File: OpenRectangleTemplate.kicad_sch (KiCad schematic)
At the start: 40 parts, among them J1 USB C Connector, J2 JTAG_TC2030, SW1 Boot, U1 XC6206, U2 USBLC6-2SC6, U3 RP2040, U4 W25Q128JVS, Y1 12MHz

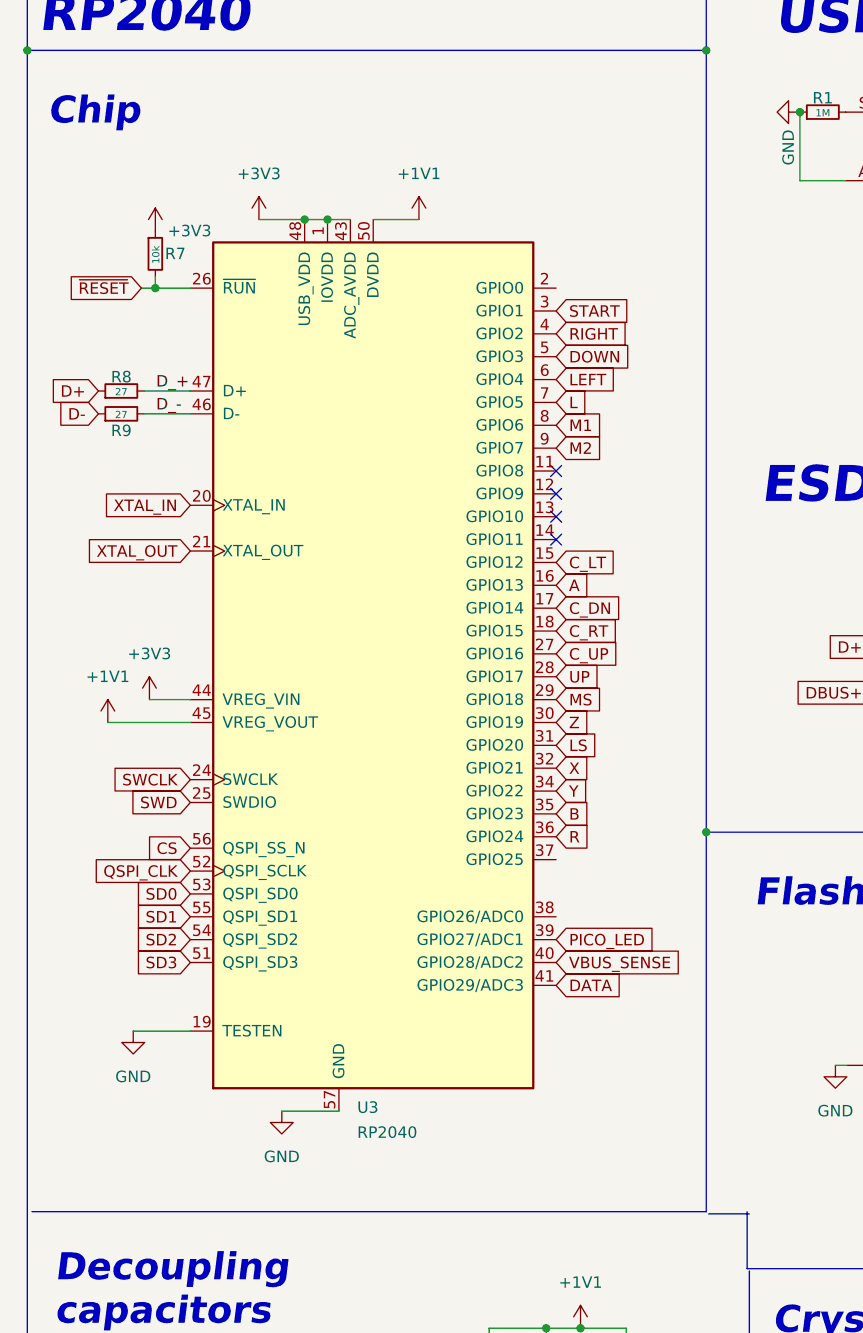
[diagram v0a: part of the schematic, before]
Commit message: Reverted back to pico pinout
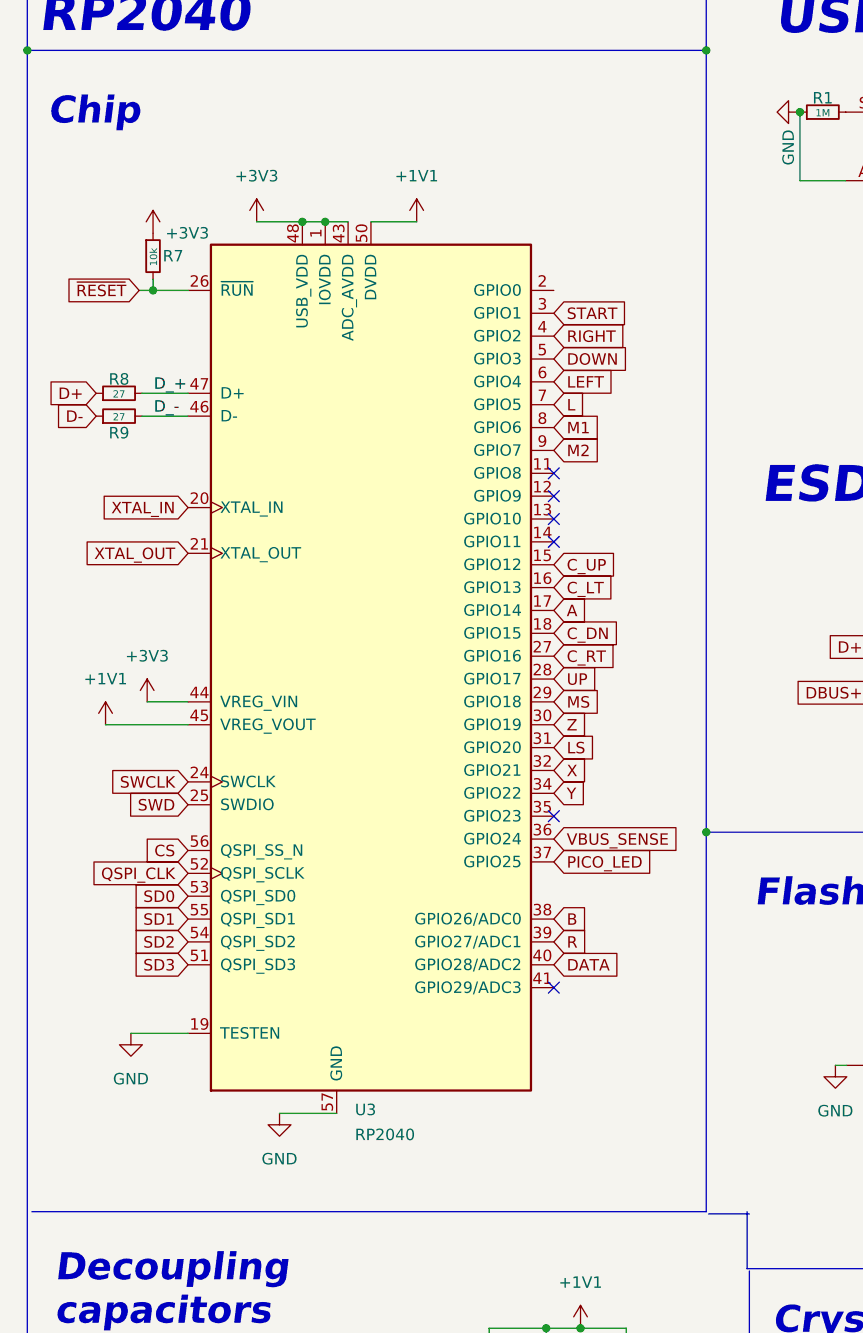
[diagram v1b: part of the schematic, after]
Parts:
- D1, D2: footprint qw-footprints:CUSTOM D_SOD-123 -> Diode_SMD:D_SOD-123
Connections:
- net A: now also U3.17 (GPIO14); no longer U3.16 (GPIO13)
- net B: now also U3.38 (GPIO26/ADC0); no longer U3.35 (GPIO23)
- net C_DN: now also U3.18 (GPIO15); no longer U3.17 (GPIO14)
- net C_LT: now also U3.16 (GPIO13); no longer U3.15 (GPIO12)
- net C_RT: now also U3.27 (GPIO16); no longer U3.18 (GPIO15)
- net C_UP: now also U3.15 (GPIO12); no longer U3.27 (GPIO16)
- net DATA: now also U3.40 (GPIO28/ADC2); no longer U3.41 (GPIO29/ADC3)
- net PICO_LED: now also U3.37 (GPIO25); no longer U3.39 (GPIO27/ADC1)
- net R: now also U3.39 (GPIO27/ADC1); no longer U3.36 (GPIO24)
- net VBUS_SENSE: now also U3.36 (GPIO24); no longer U3.40 (GPIO28/ADC2)
- no-connect marks 9 -> 11

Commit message: Prototyped and tested
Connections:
- net START: now also U3.2 (GPIO0); no longer U3.3 (GPIO1)
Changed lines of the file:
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@@
     )
   )
-  (global_label "START" (shape input) (at 71.7108 51.308 0) (fields_autoplaced)
+  (global_label "START" (shape input) (at 71.7108 48.768 0) (fields_autoplaced)
     (effects (font (size 1.27 1.27)) (justify left))
-    (property "Intersheetrefs" "${INTERSHEET_REFS}" (at 79.6272 51.2286 0)
+    (property "Intersheetrefs" "${INTERSHEET_REFS}" (at 79.6272 48.6886 0)
       (effects (font (size 1.27 1.27)) (justify left) hide)
     )

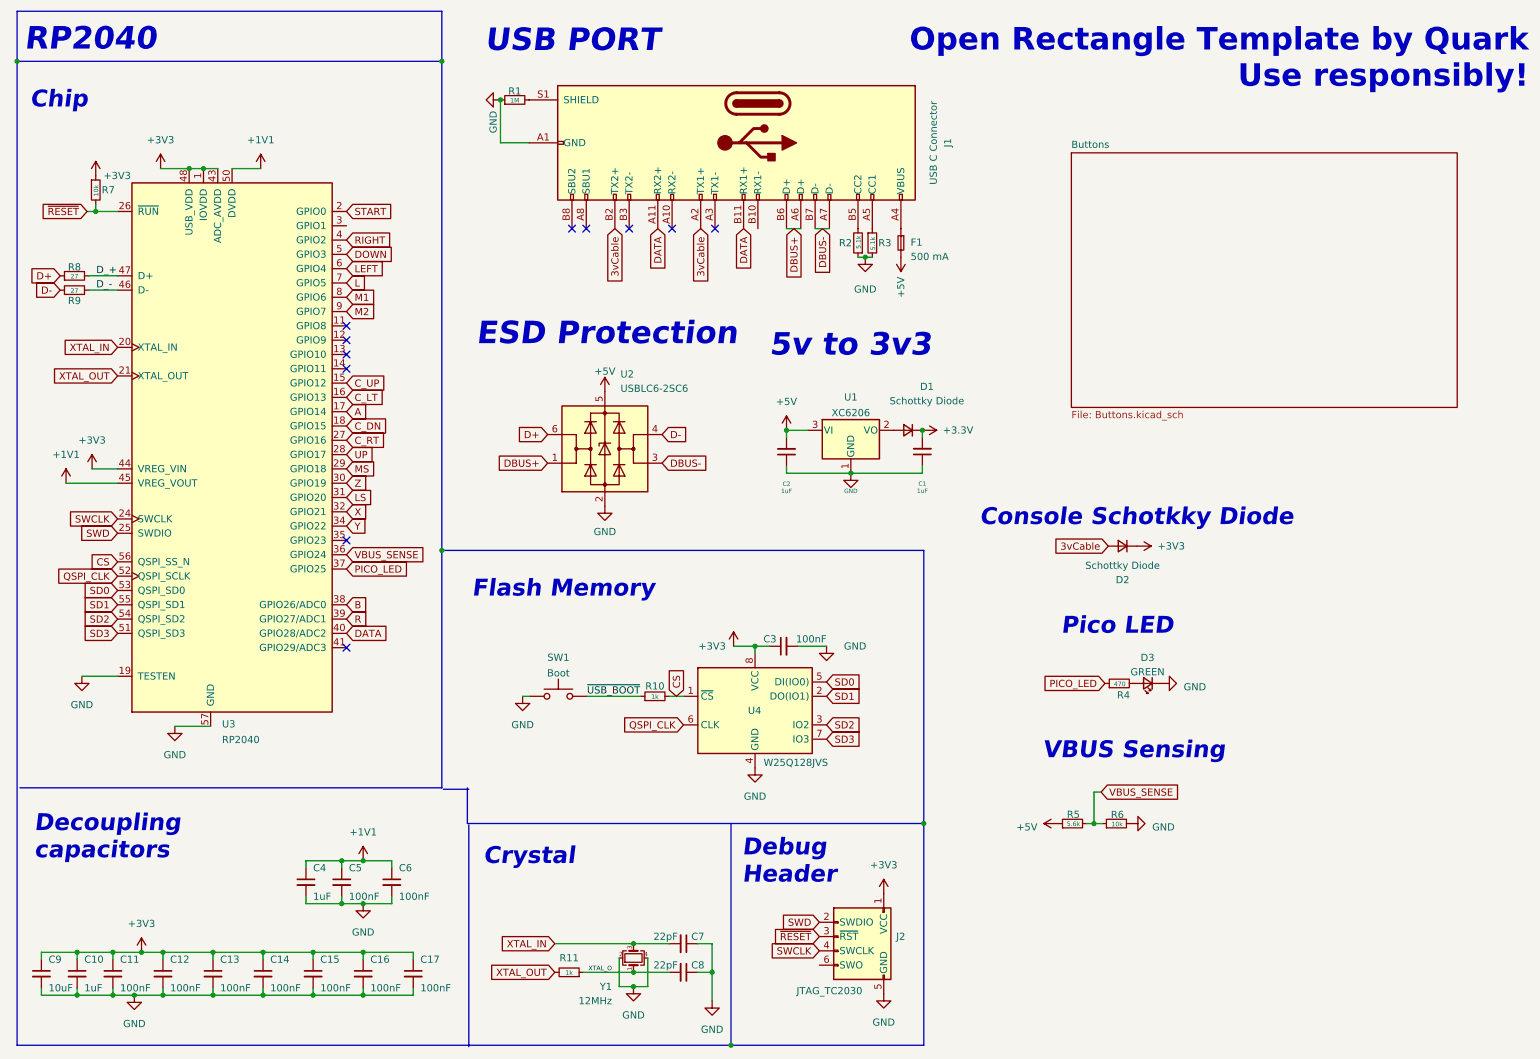
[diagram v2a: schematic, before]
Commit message: Adjusted the schematic to the correct grid
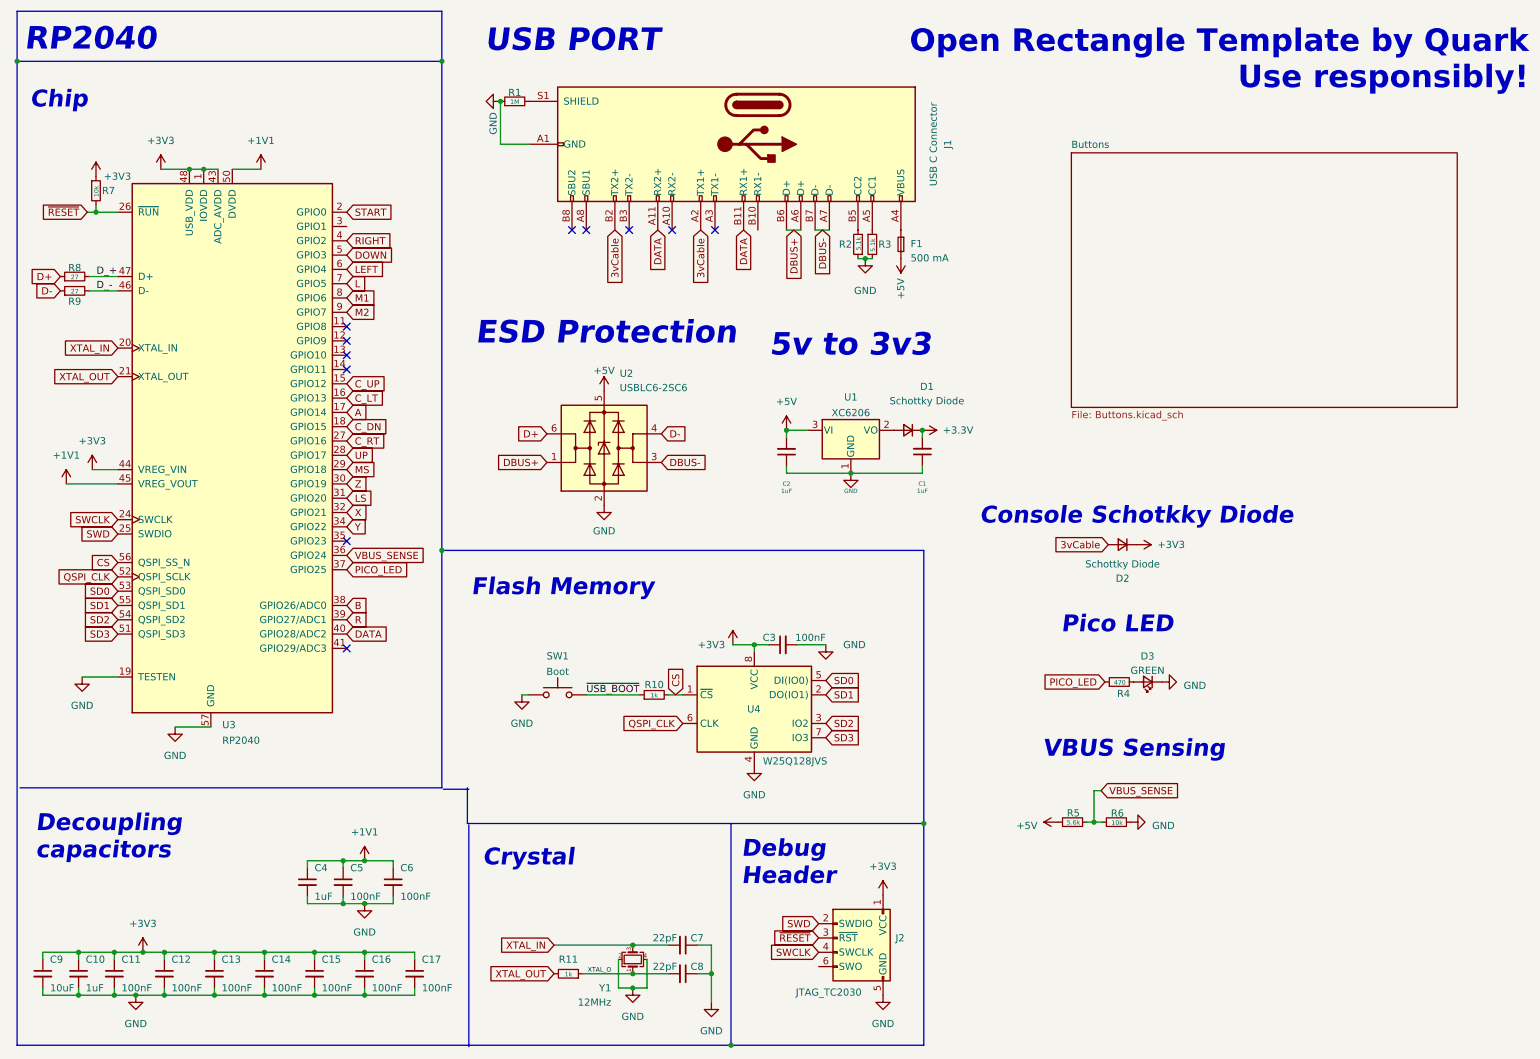
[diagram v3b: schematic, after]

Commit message: Adjusted part numbers
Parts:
- D1, D2: LCSC C130880 -> C8598
- D3: LCSC (none) -> C2297
- F1: LCSC (none) -> C70076
- R4: LCSC (none) -> C25744
- R5: LCSC (none) -> C23189
- R6: LCSC (none) -> C23192
- SW1: LCSC C5156480 -> C318884
- U2: LCSC (none) -> C7519
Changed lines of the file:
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@@
+      (effects (font (size 1.27 1.27)) hide)
+    )
+    (property "LCSC" "C23189" (at 201.9647 155.6231 0)
       (effects (font (size 1.27 1.27)) hide)
     )
@@
       (effects (font (size 1.27 1.27)) hide)
     )
+    (property "LCSC" "C70076" (at 171.9072 54.5084 0)
+      (effects (font (size 1.27 1.27)) hide)
+    )
     (pin "1")
     (pin "2")
@@
       (effects (font (size 1.27 1.27)) hide)
     )
-    (property "LCSC" "C130880" (at 171.45 87.63 0)
+    (property "LCSC" "C8598" (at 171.45 87.63 0)
       (effects (font (size 1.27 1.27)) hide)
     )
@@
       (effects (font (size 1.27 1.27)) hide)
     )
+    (property "LCSC" "C23192" (at 209.7949 155.6531 0)
+      (effects (font (size 1.27 1.27)) hide)
+    )
     (pin "1")
     (pin "2")
@@
       (effects (font (size 1.27 1.27)) hide)
     )
-    (property "LCSC" "C130880" (at 209.55 107.95 0)
+    (property "LCSC" "C8598" (at 209.55 107.95 0)
       (effects (font (size 1.27 1.27)) hide)
     )
@@
     )
     (property "Datasheet" "~" (at 214.0458 132.334 90)
+      (effects (font (size 1.27 1.27)) hide)
+    )
+    (property "LCSC" "C2297" (at 213.9823 127.762 0)
       (effects (font (size 1.27 1.27)) hide)
     )
@@
       (effects (font (size 1.27 1.27)) hide)
     )
+    (property "LCSC" "C25744" (at 210.8765 134.4111 0)
+      (effects (font (size 1.27 1.27)) hide)
+    )
     (pin "1")
     (pin "2")
@@
       (effects (font (size 1.27 1.27)) hide)
     )
-    (property "LCSC" "C5156480" (at 109.22 134.62 0)
+    (property "LCSC" "C318884" (at 109.22 134.62 0)
       (effects (font (size 1.27 1.27)) hide)
     )
@@
       (effects (font (size 1.27 1.27)) hide)
     )
+    (property "LCSC" "C7519" (at 120.2437 77.5462 0)
+      (effects (font (size 1.27 1.27)) hide)
+    )

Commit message: Updated 3D models and footprints
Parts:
- J2: footprint marbastlib-various:CON_TC2030_outlined -> PCM_marbastlib-various:CON_TC2030_outlined
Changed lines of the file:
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@@
       (effects (font (size 1.27 1.27)) (justify left))
     )
-    (property "Footprint" "marbastlib-various:CON_TC2030_outlined" (at 172.085 179.07 90)
+    (property "Footprint" "PCM_marbastlib-various:CON_TC2030_outlined" (at 172.085 179.07 90)
       (effects (font (size 1.27 1.27)) hide)
     )

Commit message: Actually a template now
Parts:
- J2: now left out of the parts list
- R1: LCSC C25190 -> C22935
- R2, R3: LCSC C25744 -> C25905
- R4: value 470 -> 10k
- R6: LCSC C23192 -> C25804
- SW1: now in the parts list
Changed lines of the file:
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@@
   )
   (symbol (lib_id "marbastlib-various:JTAG_TC2030") (at 161.925 180.34 0) (unit 1)
-    (in_bom yes) (on_board yes) (dnp no)
+    (in_bom no) (on_board yes) (dnp no)
     (property "Reference" "J2" (at 169.2148 177.7999 0)
       (effects (font (size 1.27 1.27)) (justify left))
@@
       (effects (font (size 1.27 1.27)) hide)
     )
-    (property "LCSC" "C25744" (at 162.56 54.61 0)
+    (property "LCSC" "C25905" (at 162.56 54.61 0)
       (effects (font (size 1.27 1.27)) hide)
     )
@@
       (effects (font (size 1.27 1.27)) hide)
     )
-    (property "LCSC" "C23192" (at 209.7949 155.6531 0)
+    (property "LCSC" "C25804" (at 209.7949 155.6531 0)
       (effects (font (size 1.27 1.27)) hide)
     )
@@
       (effects (font (size 1.27 1.27)) hide)
     )
-    (property "LCSC" "C25744" (at 165.1 54.61 0)
+    (property "LCSC" "C25905" (at 165.1 54.61 0)
       (effects (font (size 1.27 1.27)) hide)
     )
@@
       (effects (font (size 1.27 1.27)) (justify left))
     )
-    (property "Value" "470" (at 210.0998 132.4456 90)
+    (property "Value" "10k" (at 210.0998 132.4456 90)
       (effects (font (size 0.8 0.8)) (justify left))
     )
@@
   )
   (symbol (lib_id "Switch:SW_Push") (at 109.22 134.62 0) (unit 1)
-    (in_bom no) (on_board yes) (dnp no) (fields_autoplaced)
+    (in_bom yes) (on_board yes) (dnp no) (fields_autoplaced)
     (property "Reference" "SW1" (at 109.22 127.7325 0)
       (effects (font (size 1.27 1.27)))
@@
       (effects (font (size 1.27 1.27)) hide)
     )
-    (property "LCSC" "C25190" (at 101.6 29.21 0)
-      (effects (font (size 1.27 1.27)) hide)
-    )
+    (property "LCSC" "C22935" (at 101.6 29.21 0)
+      (effects (font (size 1.27 1.27)) hide)
+    )
